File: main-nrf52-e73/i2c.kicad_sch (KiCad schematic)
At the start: 7 parts, among them U5 AT24CS64-MAHM, U6 SHT30-DIS, U7 LIS2DE12

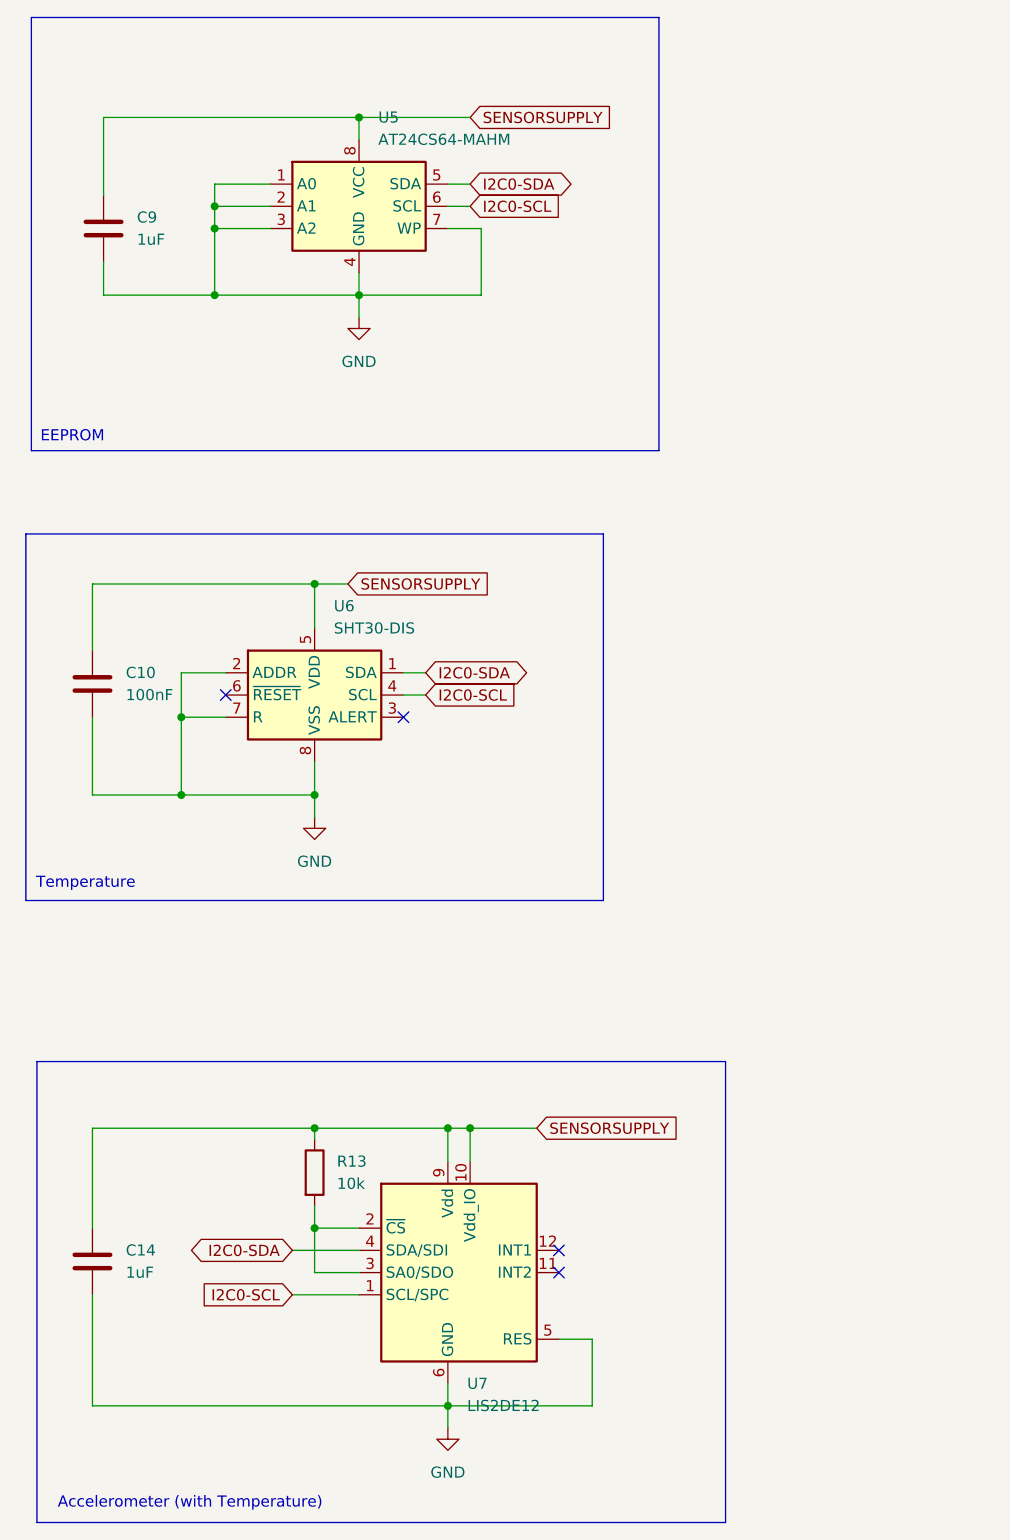
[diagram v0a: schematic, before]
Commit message: Finished first prototype of nRF52 powered main PCB.
Using Ebyte E73 module for the nRF chip.
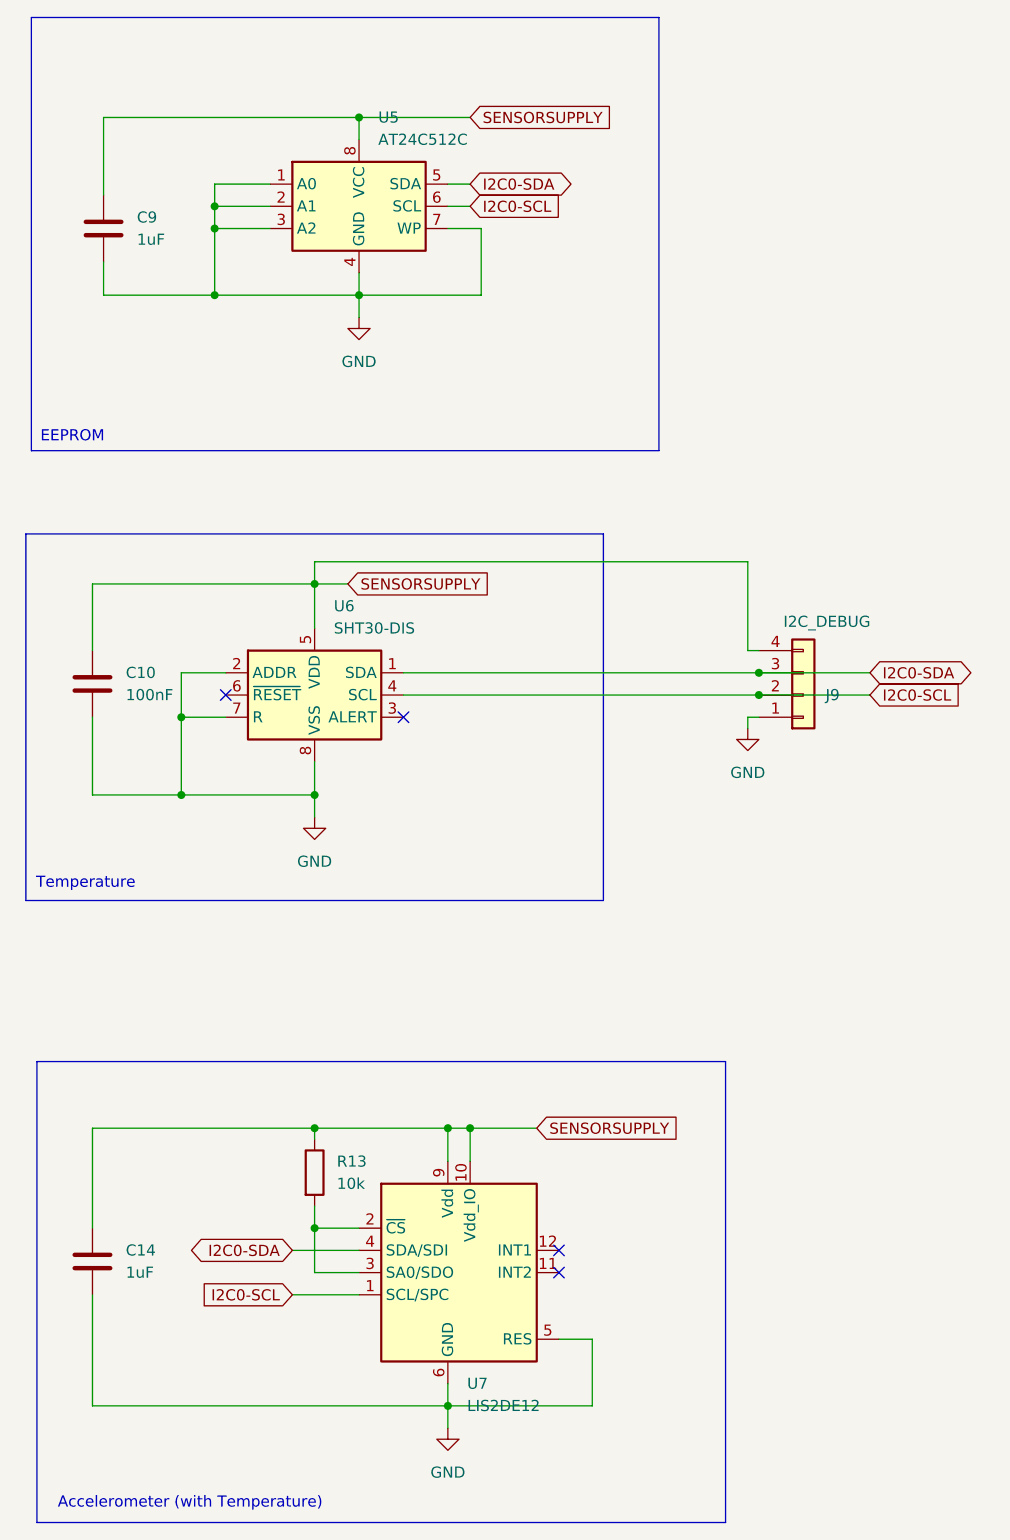
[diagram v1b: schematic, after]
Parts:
- added J9: I2C_DEBUG, Connector_PinHeader_2.54mm:PinHeader_1x04_P2.54mm_Vertical, symbol Connector_Generic:Conn_01x04
- C10: footprint Capacitor_SMD:C_0805_2012Metric -> Capacitor_SMD:C_0603_1608Metric; LCSC (none) -> C14663
- C14, C9: LCSC (none) -> C28323
- R13: LCSC (none) -> C25804
- U5: value AT24CS64-MAHM -> AT24C512C; footprint Package_DFN_QFN:DFN-8-1EP_3x2mm_P0.5mm_EP1.3x1.5mm -> Package_SO:SOIC-8_3.9x4.9mm_P1.27mm; LCSC (none) -> C12371
- U6: LCSC (none) -> C77361
- U7: LCSC (none) -> C110926
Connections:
- net GND: now also J9.1 (Pin_1)
- net I2C0-SCL: now also J9.2 (Pin_2)
- net I2C0-SDA: now also J9.3 (Pin_3)
- net SENSORSUPPLY: now also J9.4 (Pin_4)
